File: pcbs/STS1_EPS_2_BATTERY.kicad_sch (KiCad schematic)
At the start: 23 parts, among them J9 Battery Pack, Q23 SI7272DP-T1-GE3, U6 TPS2420RSAT, U7 BQ29209DRBT, U9 4002

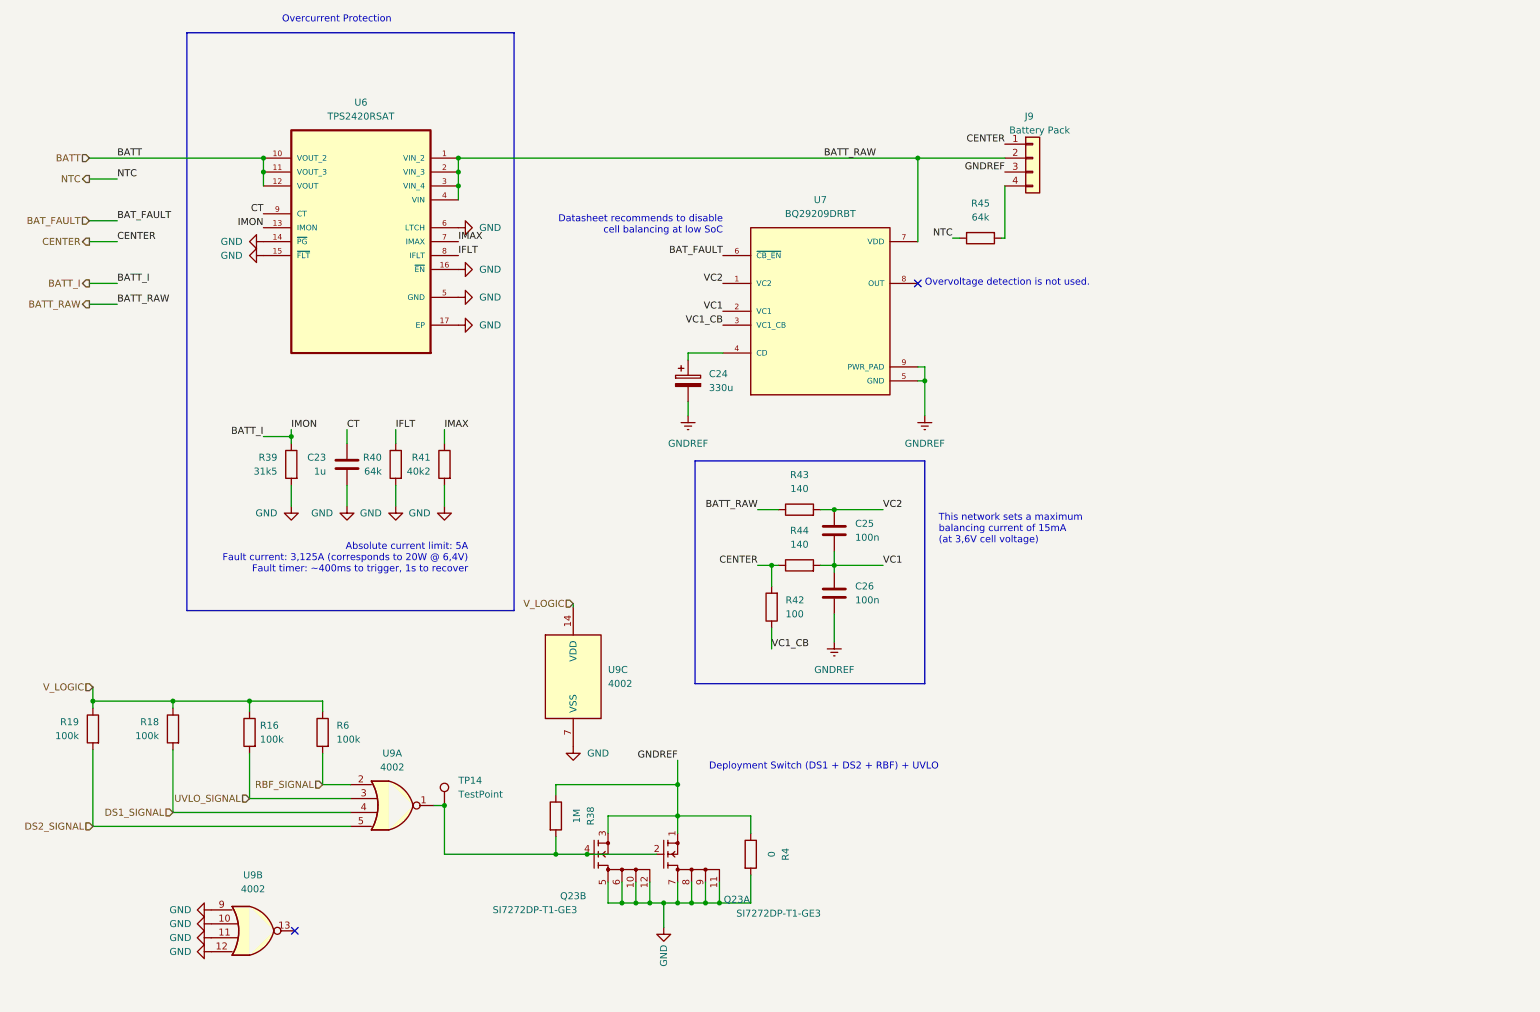
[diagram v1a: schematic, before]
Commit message: Ported kicad projects to KiCad 8.0.
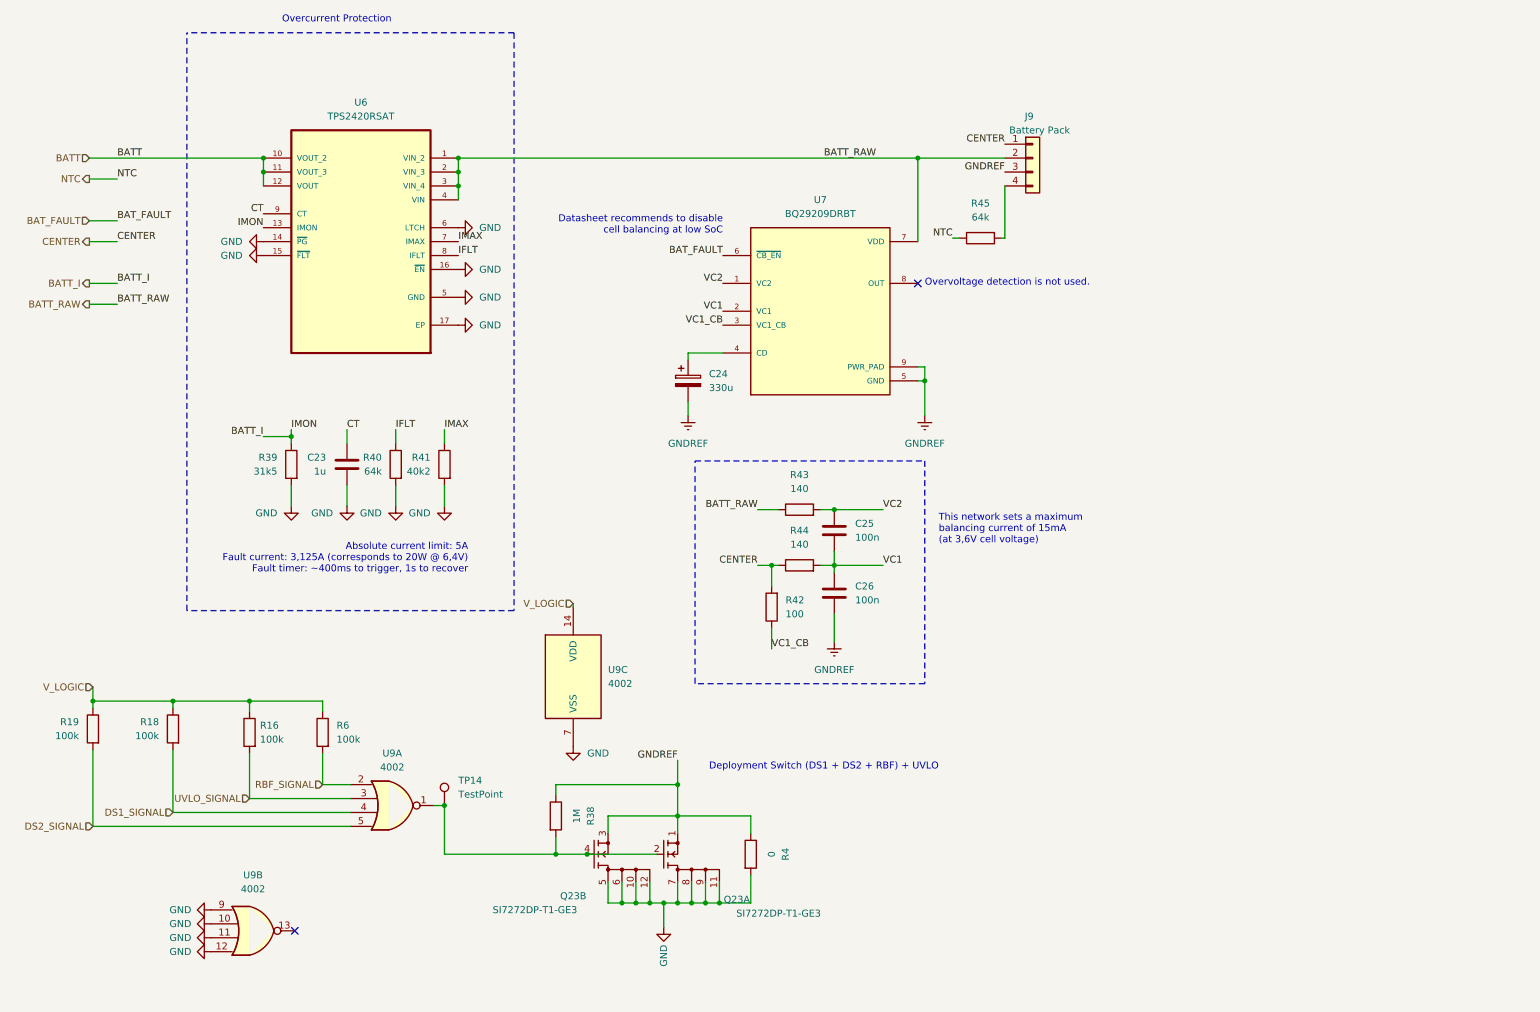
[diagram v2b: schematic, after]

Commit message: Changed some footprints that had the wrong shape in EPS 2.1.
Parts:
- U6: footprint Package_DFN_QFN:VQFN-16-1EP_3x3mm_P0.5mm_EP1.45x1.45mm_ThermalVias -> STS_Package_DFN_QFN:QFN65P400X400X100-17N
- U9: footprint Package_SO:SOIC-14_3.9x8.7mm_P1.27mm -> STS_Misc:SOP127P780X200-14N
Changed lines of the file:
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@@
 			)
 		)
-		(property "Footprint" "Package_DFN_QFN:VQFN-16-1EP_3x3mm_P0.5mm_EP1.45x1.45mm_ThermalVias"
+		(property "Footprint" "STS_Package_DFN_QFN:QFN65P400X400X100-17N"
 			(at 75.565 54.61 0)
 			(effects
@@
 			)
 		)
-		(property "Footprint" "Package_SO:SOIC-14_3.9x8.7mm_P1.27mm"
+		(property "Footprint" "STS_Misc:SOP127P780X200-14N"
 			(at 81.28 160.02 0)
 			(effects
@@
 			)
 		)
-		(property "Footprint" "Package_SO:SOIC-14_3.9x8.7mm_P1.27mm"
+		(property "Footprint" "STS_Misc:SOP127P780X200-14N"
 			(at 114.3 136.525 0)
 			(effects
@@
 			)
 		)
-		(property "Footprint" "Package_SO:SOIC-14_3.9x8.7mm_P1.27mm"
+		(property "Footprint" "STS_Misc:SOP127P780X200-14N"
 			(at 55.88 182.88 0)
 			(effects

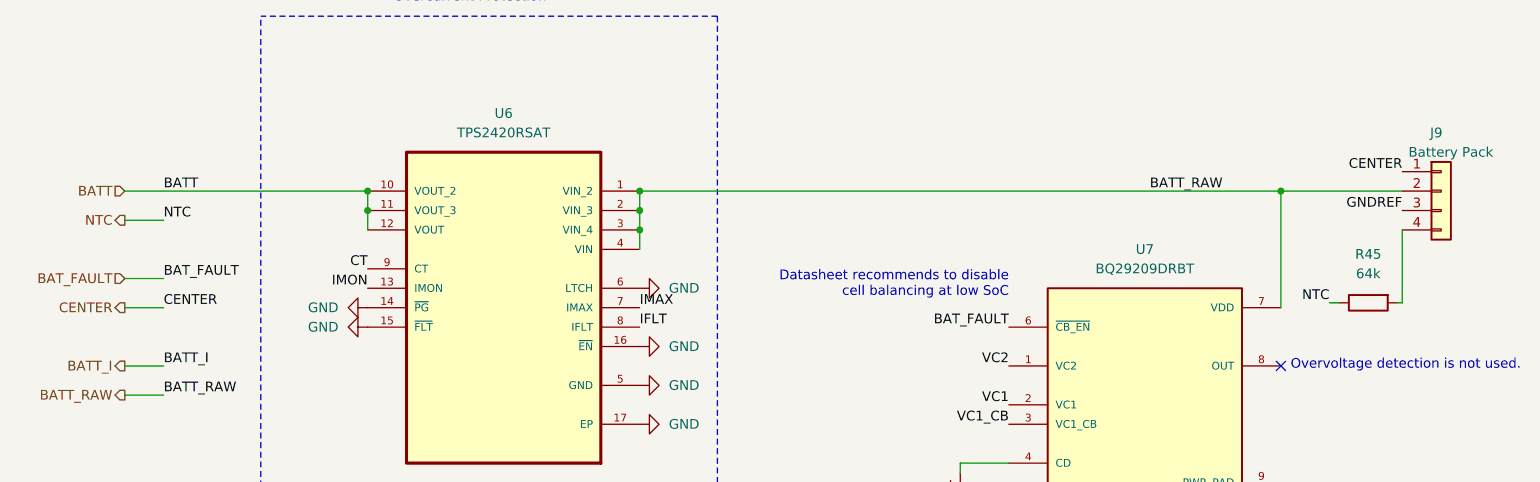
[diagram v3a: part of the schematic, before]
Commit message: Added test point directly at battery and after switch.
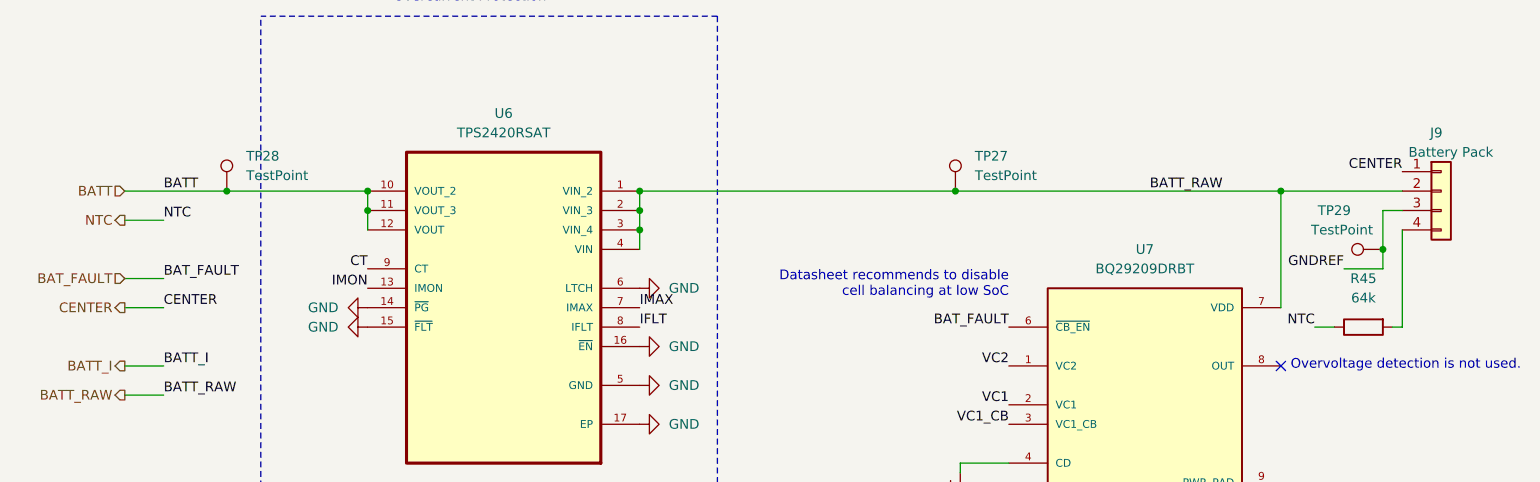
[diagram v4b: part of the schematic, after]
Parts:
- added TP27, TP28, TP29: TestPoint, TestPoint:TestPoint_THTPad_D1.0mm_Drill0.5mm, symbol Connector:TestPoint
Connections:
- net BATT: now also TP28.1
- net BATT_RAW: now also TP27.1
- net GNDREF: now also TP29.1
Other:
- moved on the sheet: R45

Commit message: Intermediate commit.
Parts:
- removed Q23: SI7272DP-T1-GE3, STS_Package_SO:POWERPAK_SO8, symbol STS_Transistor_FET:SI7272DP-T1-GE3
- removed R38: 1M, Resistor_SMD:R_0805_2012Metric, symbol Device:R
- removed R4: 0, Resistor_SMD:R_0805_2012Metric, symbol Device:R
- removed U9: 4002, STS_Misc:SOP127P780X200-14N, symbol 4xxx:4002
- added U1: 4072, Package_SO:SOIC-14_3.9x8.7mm_P1.27mm, symbol 4xxx_IEEE:4072
- added U9: 4072, symbol 4xxx_IEEE:4072
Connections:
- net DS1_SIGNAL: now also U1.4
- net DS2_SIGNAL: now also U1.12
- net GND: now also C26.2, U7.5 (GND), U7.9 (PWR_PAD), U1.7 (Vss), U9.10, U9.11, U9.12, U9.7 (Vss), U9.9; no longer U6.16 (~{EN})
- net GNDREF: no longer C26.2, U7.5 (GND), U7.9 (PWR_PAD)
- net RBF_SIGNAL: now also U1.2
- net UVLO_SIGNAL: now also U1.3
- net V_LOGIC: now also U1.14 (Vdd), U9.14 (Vdd)
- net ~{BATT_INHIBIT}: now reaches TP14.1
- net ~{BATT_INHIBIT}: now also U6.16 (~{EN}), U1.1
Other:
- note added: "Absolute current limit: 5A Fault current: 3,125A (corresponds to 20W @ 6,4V) Fault timer: ~400ms to trigger, 1s to recover Is also used as power inhibit that is triggered by the DS, RBF and UVLO."
- note removed: "Absolute current limit: 5A Fault current: 3,125A (corresponds to 20W @ 6,4V) Fault timer: ~400ms to trigger, 1s to recover"
- moved on the sheet: C23, C24, C25, C26, J9, R16, R18, R39, R40, R41, R42, R43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

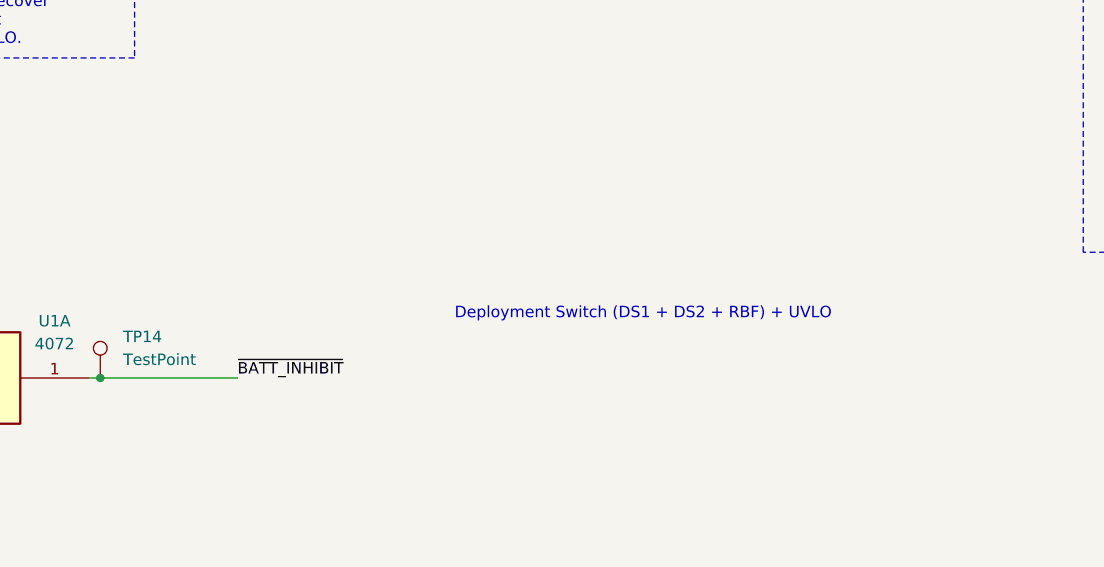
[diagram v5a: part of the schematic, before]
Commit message: Removed UCI connector from STS1_EPS_2 and merged UCI connector with J5 on STS1_EPS_1.
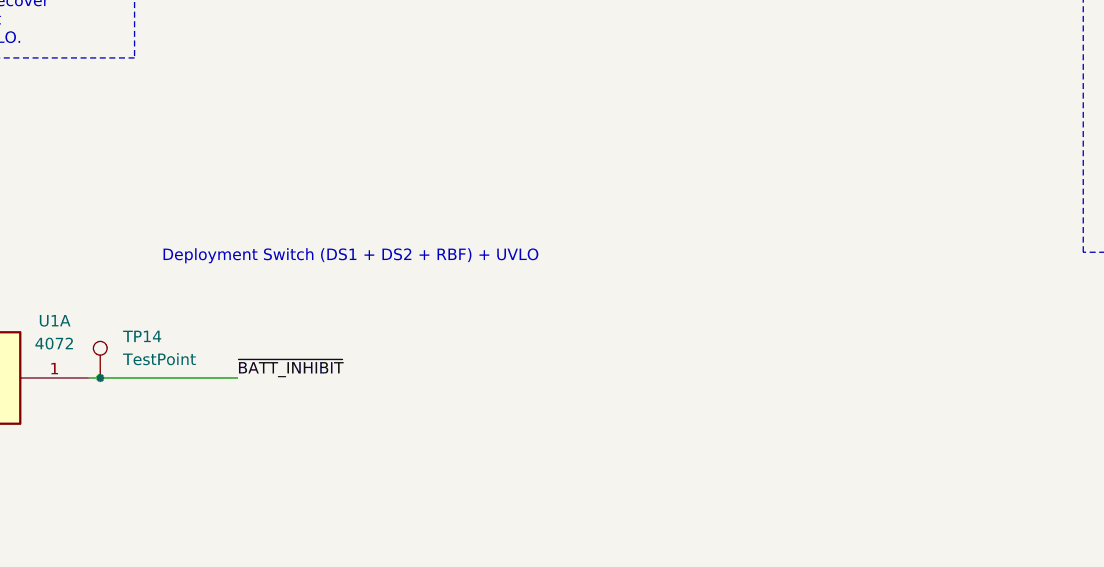
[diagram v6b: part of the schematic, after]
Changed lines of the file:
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@@
 	(text "Deployment Switch (DS1 + DS2 + RBF) + UVLO"
 		(exclude_from_sim no)
-		(at 139.7 153.67 0)
+		(at 107.188 147.32 0)
 		(effects
 			(font

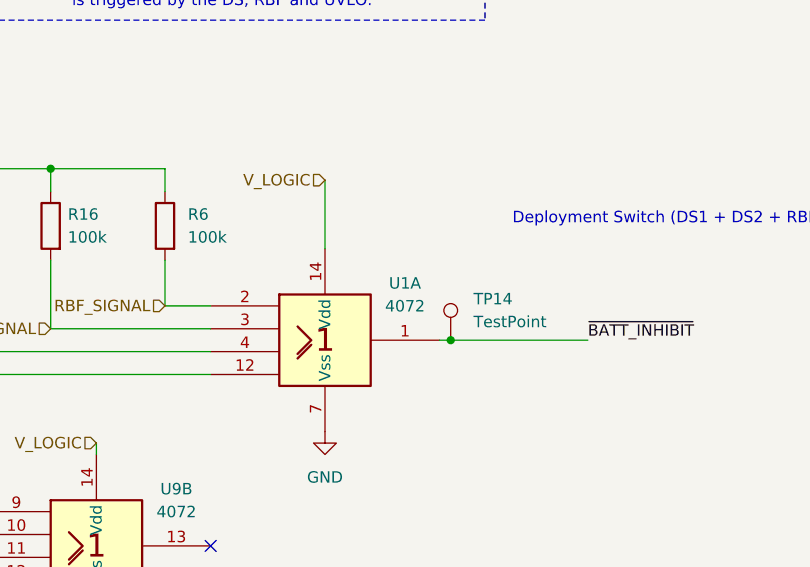
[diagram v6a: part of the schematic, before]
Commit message: Added even more ESD protection.
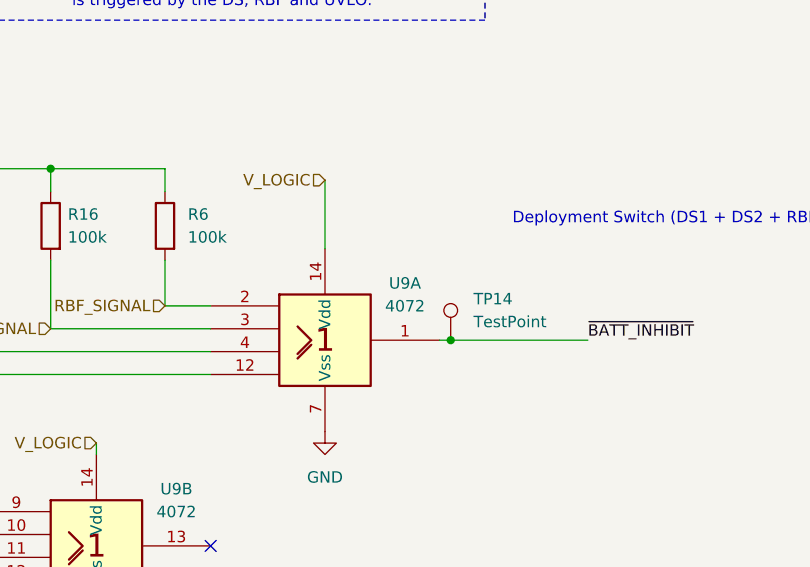
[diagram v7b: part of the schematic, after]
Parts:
- U9: footprint (none) -> Package_SO:SOIC-14_3.9x8.7mm_P1.27mm
- renumbered U1 to U9
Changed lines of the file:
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@@
 		(dnp no)
 		(fields_autoplaced yes)
-		(property "Reference" "U1"
+		(property "Reference" "U9"
 			(at 95.25 153.7014 0)
 			(effects
@@
 			(project "STS1_EPS_2"
 				(path "/38c03ff7-ea47-4d00-b37d-ddcaa7d87722/75dca64b-8858-4c1f-8340-a846cd3da1d0"
-					(reference "U1")
+					(reference "U9")
 					(unit 1)
 				)
@@
 			)
 		)
-		(property "Footprint" ""
+		(property "Footprint" "Package_SO:SOIC-14_3.9x8.7mm_P1.27mm"
 			(at 60.96 182.88 0)
 			(effects
